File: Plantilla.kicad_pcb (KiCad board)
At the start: 2 copper layers, 60 x 30 mm, 12 parts, among them J1 Screw_Terminal_01x03, Q1 IRF540N, U1 TIMER 555

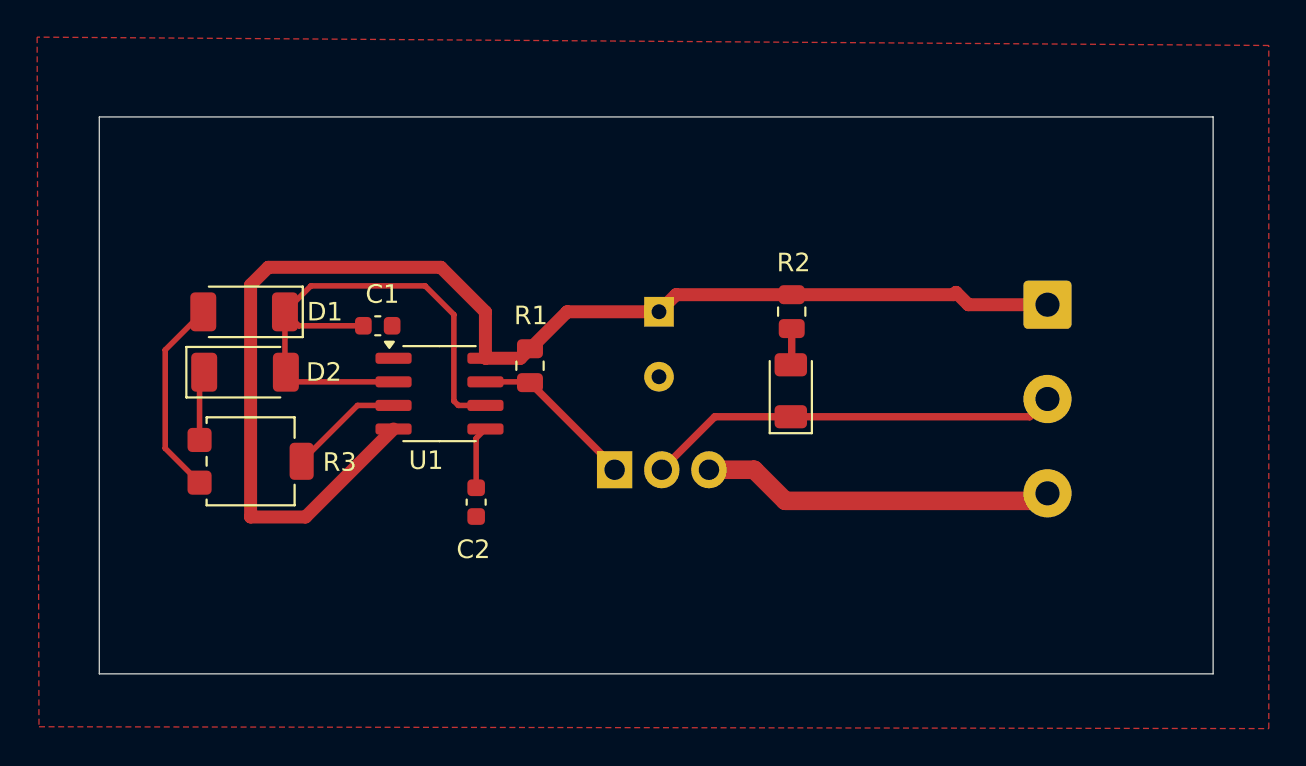
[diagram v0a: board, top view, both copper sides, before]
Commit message: Se ha redibujado la capa de relleno de cobre.
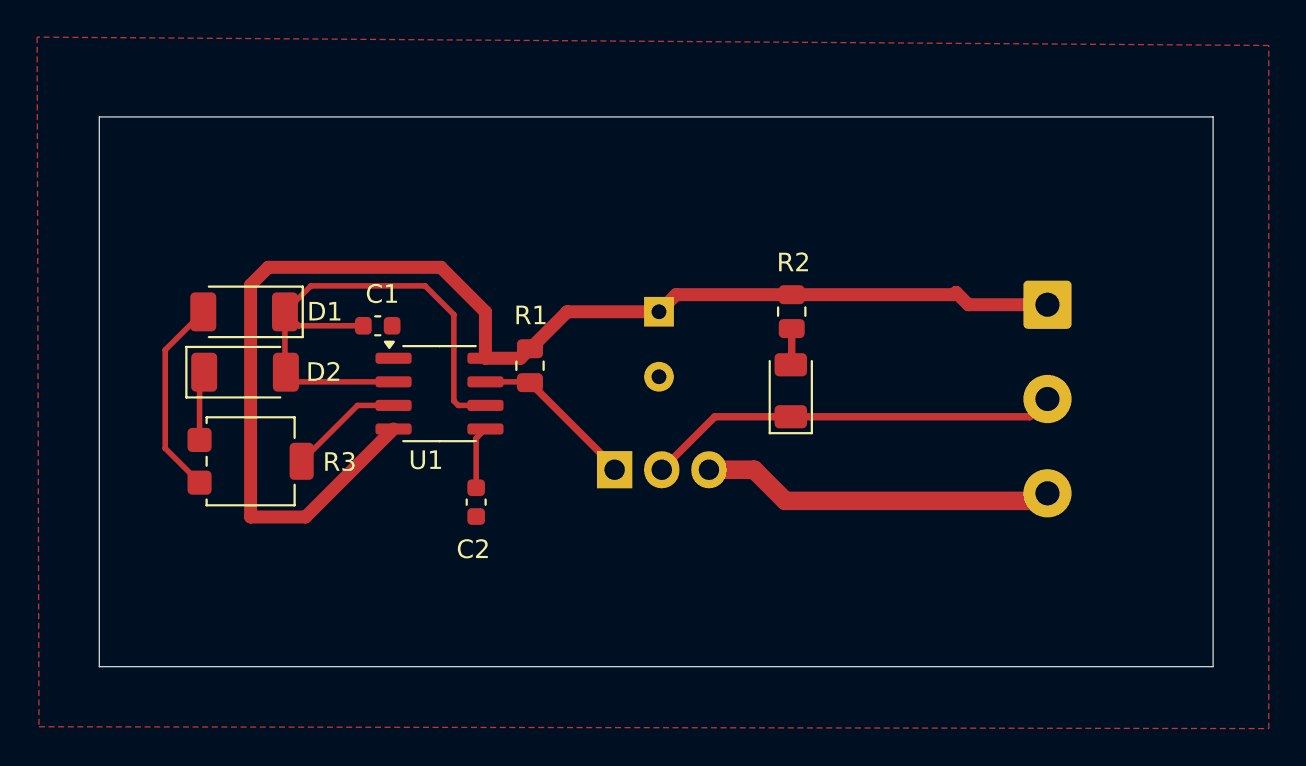
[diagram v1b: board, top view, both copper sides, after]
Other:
- board size 60 x 30 mm -> 60 x 29.6 mm
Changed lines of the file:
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@@
 	(gr_rect
 		(start 113.068398 87.337389)
-		(end 173.068398 117.337389)
+		(end 173.068398 116.949999)
 		(stroke
 			(width 0.05)

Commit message: Se ha redibujado la capa de relleno de cobre.
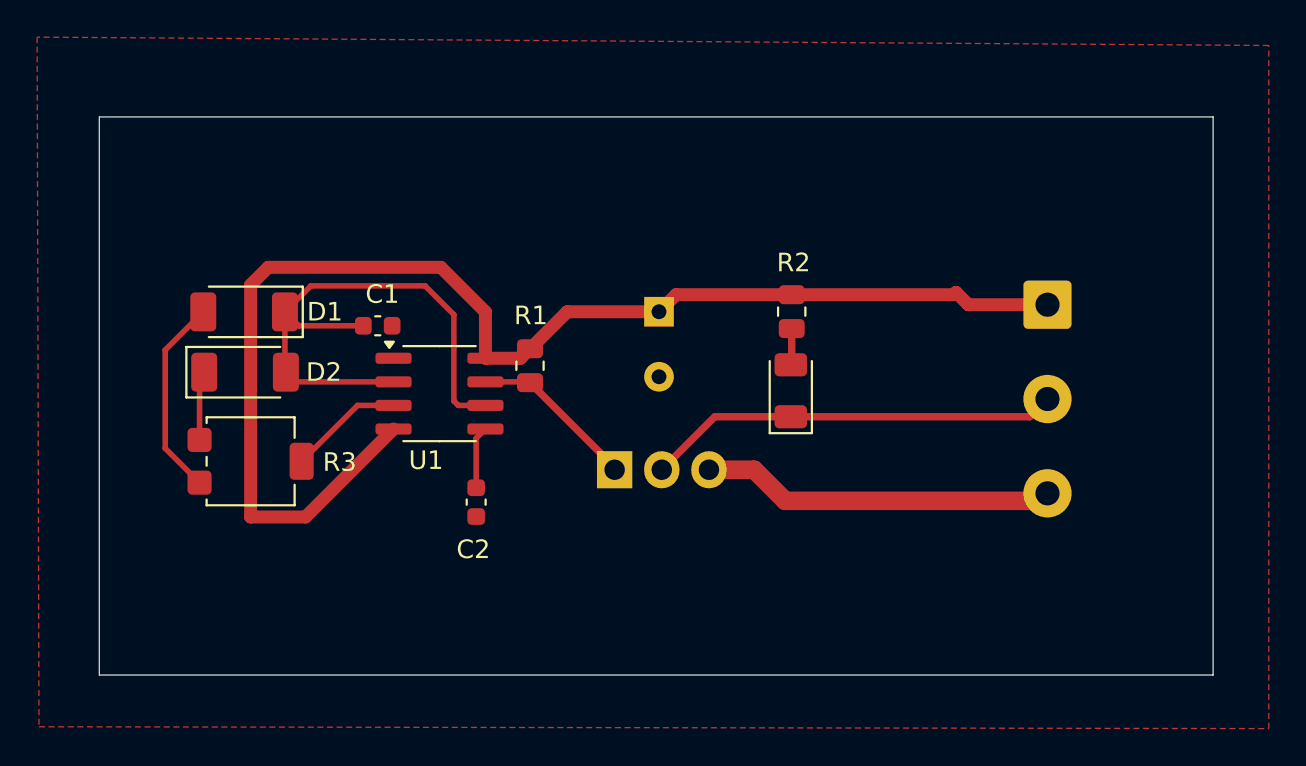
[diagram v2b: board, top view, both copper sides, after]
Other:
- board size 60 x 29.6 mm -> 60 x 30.1 mm
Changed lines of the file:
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@@
 	(gr_rect
 		(start 113.068398 87.337389)
-		(end 173.068398 116.949999)
+		(end 173.068398 117.399999)
 		(stroke
 			(width 0.05)

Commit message: Diseño actualizado con la nueva resistencia R4.
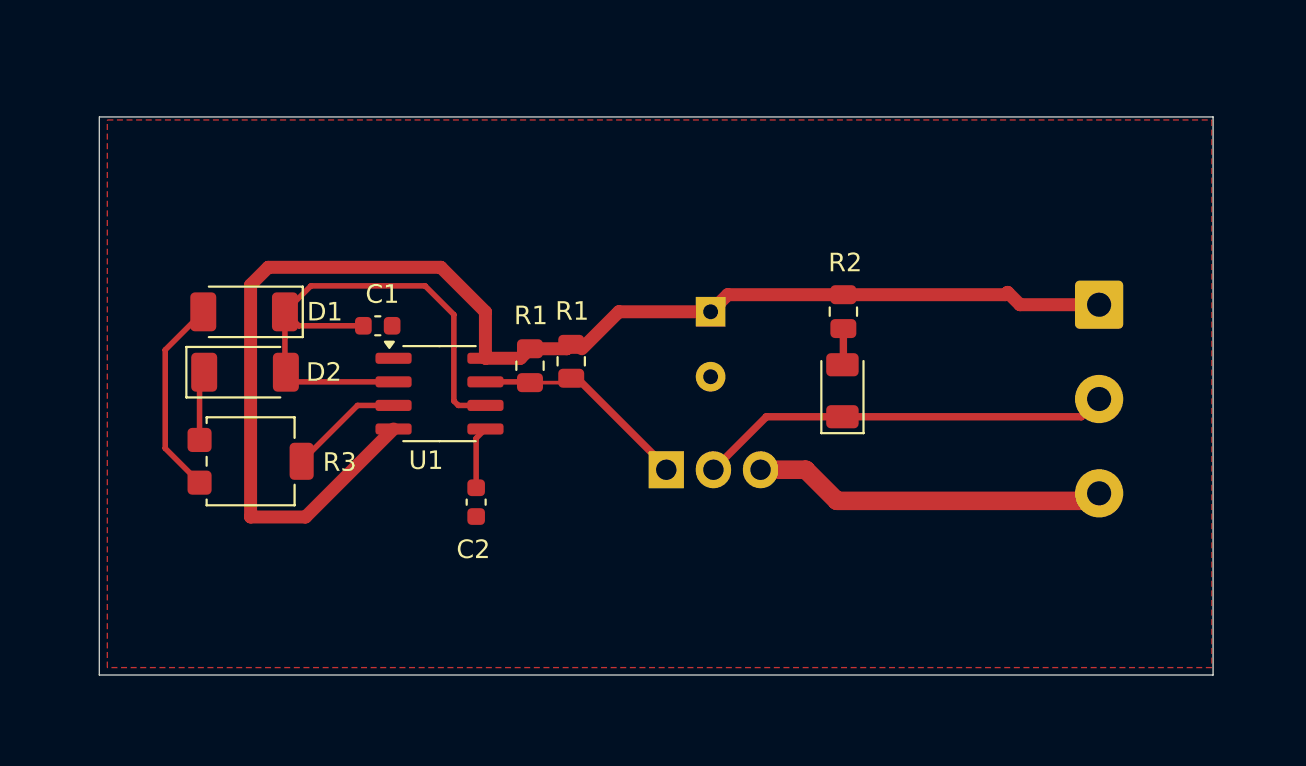
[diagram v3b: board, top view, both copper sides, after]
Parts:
- added R1: 10K, Resistor_SMD:R_0805_2012Metric, F.Cu at (138.5, 100.5)
- moved J1 2.78 mm to (166.9, 97.5)
- moved Q1 2.78 mm to (143.6, 106.3)
- moved C3 2.78 mm to (146.0, 97.8)
- moved D3 2.78 mm to (153.1, 102.1)
- moved R2 2.78 mm to (153.2, 97.8)
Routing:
- net +12V: track 70.7 -> 73.0 mm
- net Net-(Q1-G): track 8.94 -> 11.3 mm
